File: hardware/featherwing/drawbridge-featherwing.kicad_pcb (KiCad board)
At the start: 2 copper layers, 50.8 x 22.9 mm, 16 parts, among them J1 Feather 16, J2 Feather 12, J3 OUT / GND, Q1 2N3904

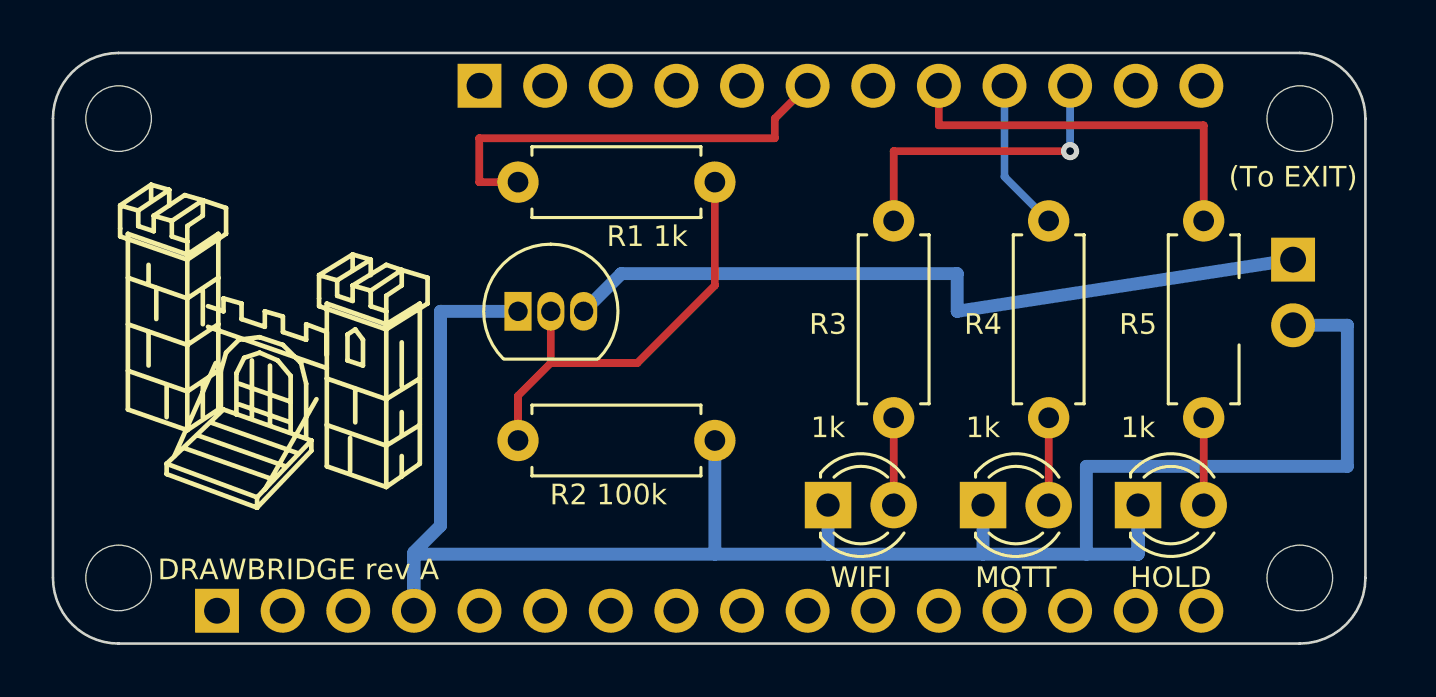
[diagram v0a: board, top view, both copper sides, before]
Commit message: Finalize FeatherWing fabrication design
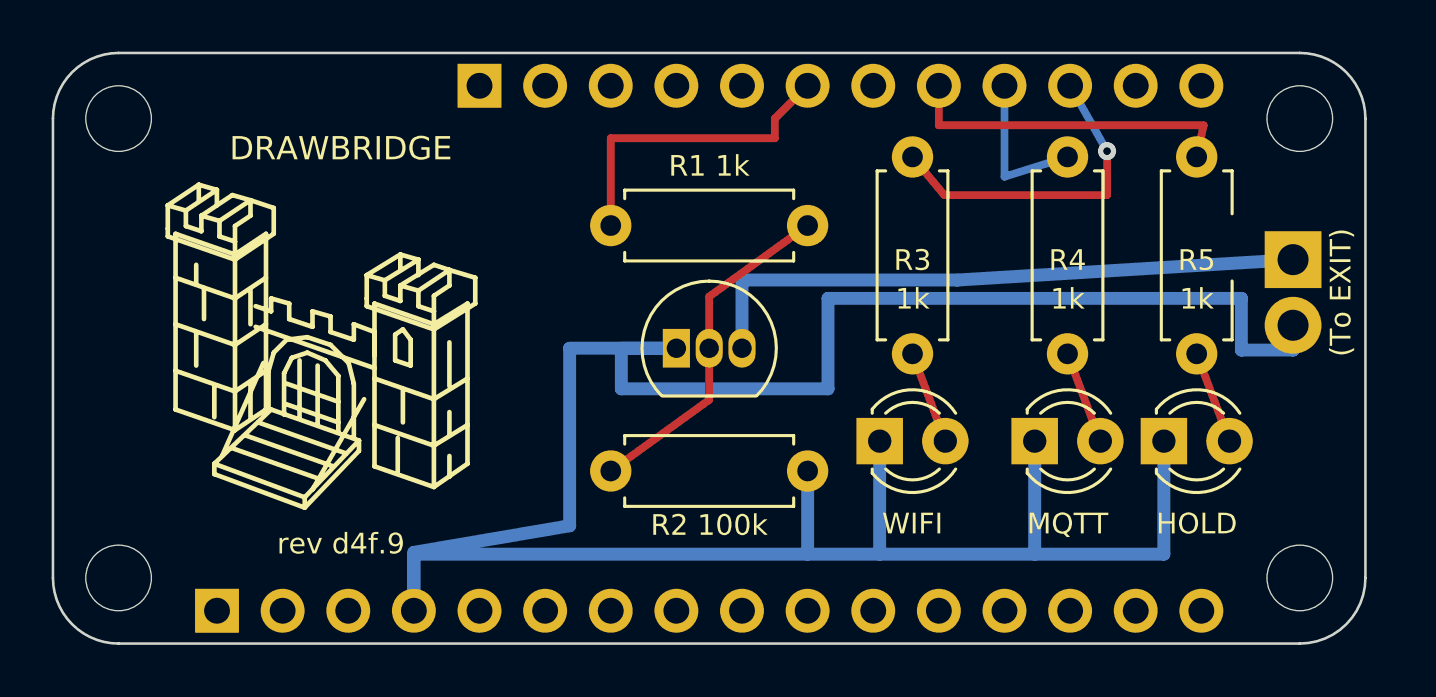
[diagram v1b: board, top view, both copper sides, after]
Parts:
- J1, J2: moved to B.Cu
- J3: footprint Drawbridge:GateOutputHeader -> Drawbridge:GateOutputPads
- moved Q1 6.29 mm to (74.1, 61.4)
- moved R1 3.96 mm to (71.6, 56.7)
- moved R2 3.78 mm to (71.6, 66.2)
- moved D1 3.18 mm to (82.0, 65.0)
- moved D2 3.18 mm to (88.0, 65.0)
- moved D3 2.67 mm to (93.0, 65.0)
- moved R3 2.58 mm to (83.3, 54.0)
- moved R4 2.58 mm to (89.3, 54.0)
- moved R5 2.49 mm to (94.3, 54.0)
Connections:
- net /CTRL_IO7 renamed /CTRL_D11
- net /HOLD_IO1 renamed /HOLD_D9
- net /MQTT_IO38 renamed /MQTT_D6
- net /WIFI_IO33 renamed /WIFI_D5
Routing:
- net /GND: track 78.3 -> 103.1 mm
- net /OUT_OC: track 29.7 -> 24.0 mm
- net /CTRL_D11: track 17.2 -> 12.3 mm
- net /BASE: track 17.1 -> 13.4 mm
- net /HOLD_D9: track 15.5 -> 13.0 mm
- net /WIFI_D5: track 12.1 -> 12.8 mm
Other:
- board text added: "DRAWBRIDGE"
- board text added: "rev d4f.9"
- board text removed: "DRAWBRIDGE rev A"

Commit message: Use a screw terminal and 45-degree routing on the FeatherWing
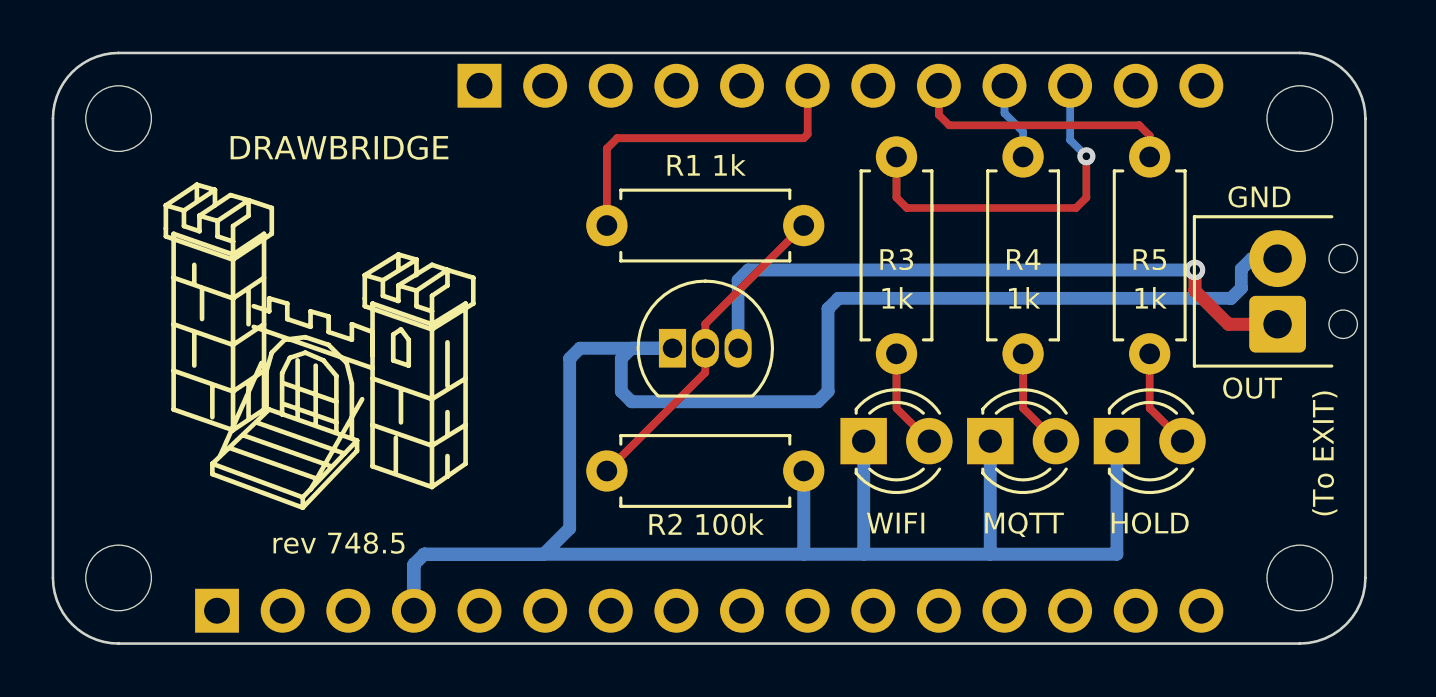
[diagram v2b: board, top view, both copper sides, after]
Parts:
- J3: footprint Drawbridge:GateOutputPads -> Drawbridge:ExitTerminal
- R5: footprint Drawbridge:GateHoldResistor -> Resistor_THT:R_Axial_DIN0207_L6.3mm_D2.5mm_P7.62mm_Horizontal
- moved J3 2.57 mm to (97.4, 60.5), turned to 90 degrees
- moved D3 1.82 mm to (91.2, 65.0)
- moved R5 1.82 mm to (92.5, 54.0)
- moved D2 1.72 mm to (86.3, 65.0)
- moved R4 1.72 mm to (87.5, 54.0)
- moved D1 0.62 mm to (81.4, 65.0)
- moved R3 0.62 mm to (82.7, 54.0)
- moved R1 0.15 mm to (71.4, 56.7)
- moved R2 0.15 mm to (71.4, 66.2)
- moved Q1 0.15 mm to (74.0, 61.4)
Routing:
- net /GND: track 103.1 -> 98.2 mm
- net /MQTT_D6: track 6.08 -> 3.05 mm
- net /HOLD_D9: track 13.0 -> 10.4 mm
- net /WIFI_D5: track 12.8 -> 13.8 mm
- net /OUT_OC: track 24.0 -> 25.0 mm, vias 0 -> 1
- net /BASE: track 13.4 -> 12.7 mm
- net /CTRL_D11: track 12.3 -> 12.9 mm
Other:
- board text added: "GND"
- board text added: "OUT"
- board text added: "rev 748.5"
- board text removed: "rev d4f.9"
